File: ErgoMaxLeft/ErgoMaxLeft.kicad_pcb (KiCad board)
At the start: 2 copper layers, 182.8 x 169.2 mm, 102 parts, among them J1 PJ-320A, K1 KEYSW, K10 KEYSW, K11 KEYSW, K12 KEYSW, K13 KEYSW, K14 KEYSW, K15 KEYSW, K16 KEYSW, K17 KEYSW, K18 KEYSW, K19 KEYSW, K2 KEYSW, K20 KEYSW, K21 KEYSW, K22 KEYSW, K23 KEYSW, K24 KEYSW, K25 KEYSW, K26 KEYSW, K27 KEYSW, K28 KEYSW, K29 KEYSW, K3 KEYSW, K30 KEYSW, K31 KEYSW, K32 KEYSW, K33 KEYSW, K34 KEYSW, K35 KEYSW, K36 KEYSW, K37 KEYSW, K38 KEYSW, K39 KEYSW, K4 KEYSW, K40 KEYSW, K41 KEYSW, K42 KEYSW, K43 KEYSW, K44 KEYSW, K5 KEYSW, K6 KEYSW, K7 KEYSW, K8 KEYSW, K9 KEYSW, U1 ProMicro

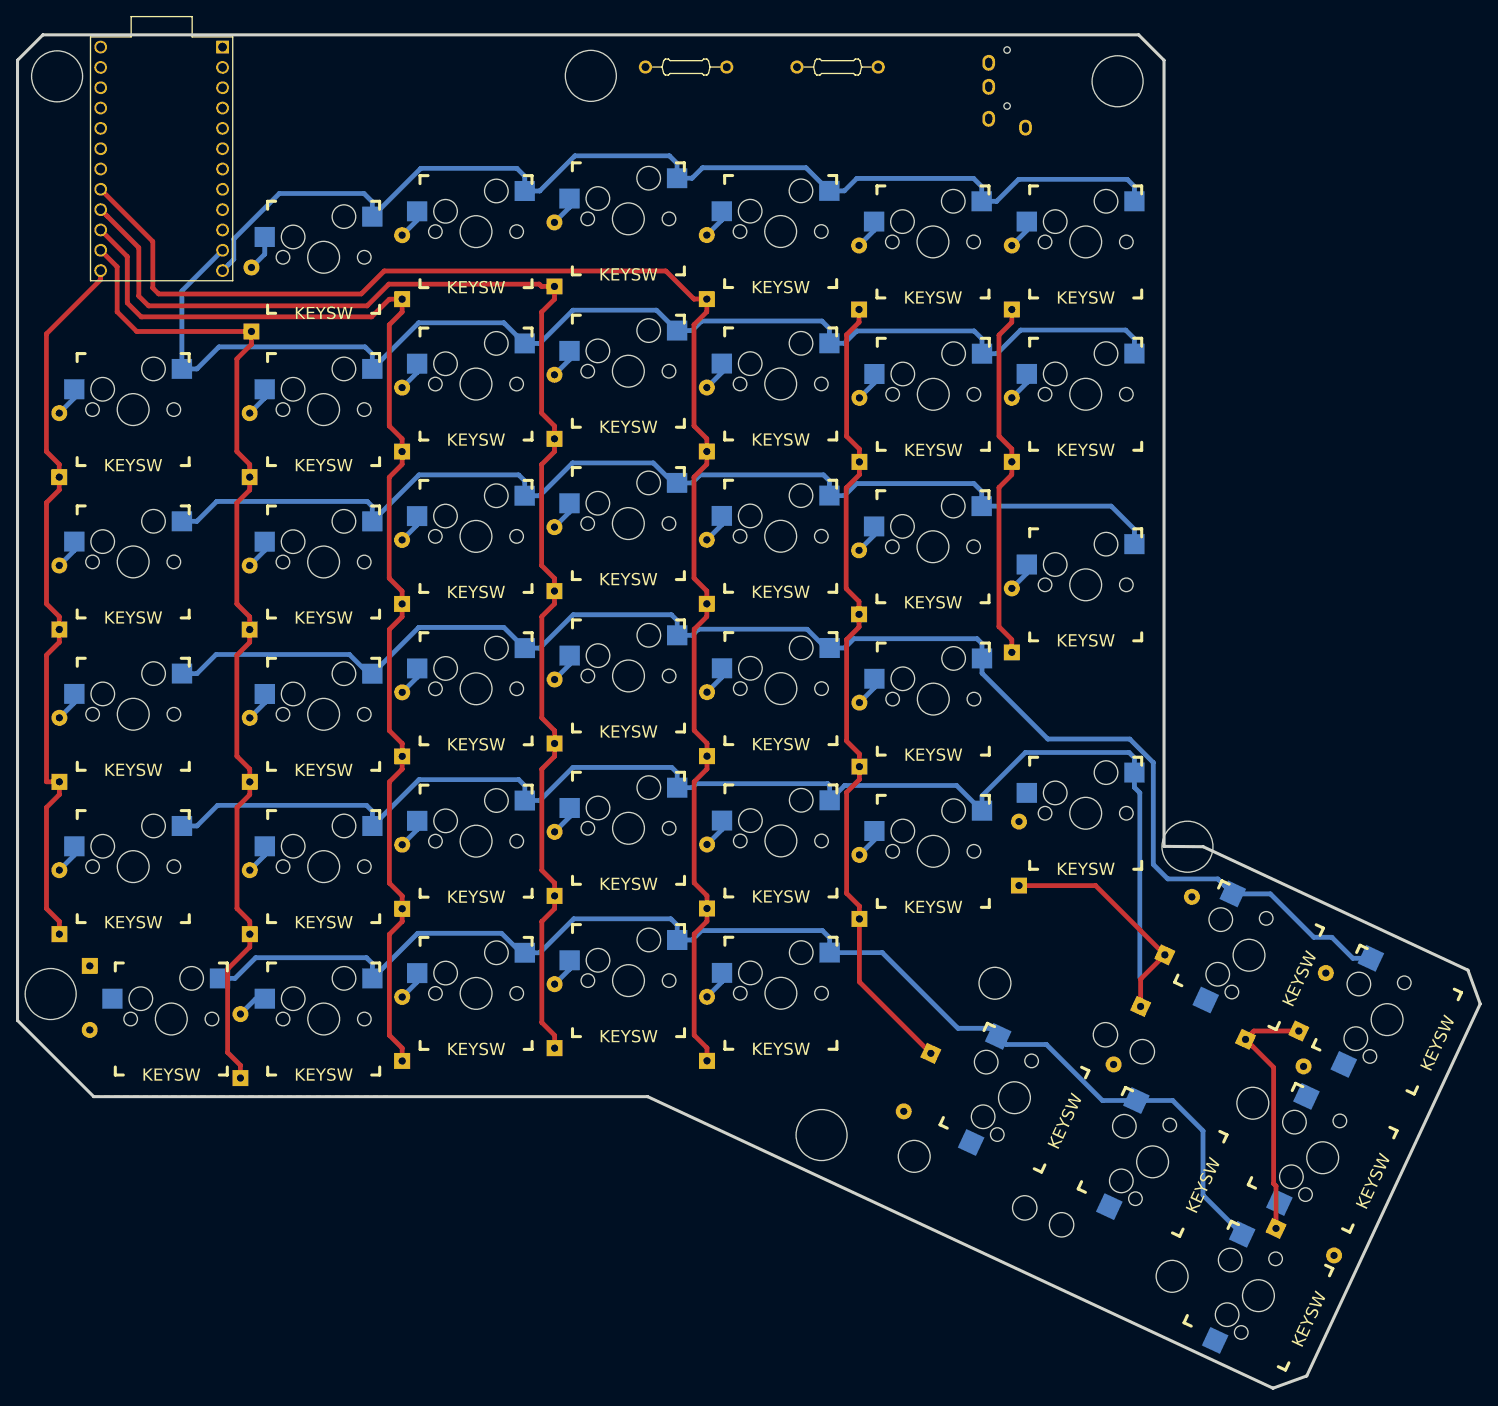
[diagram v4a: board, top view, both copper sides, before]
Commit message: finish left PCB and add 3d models
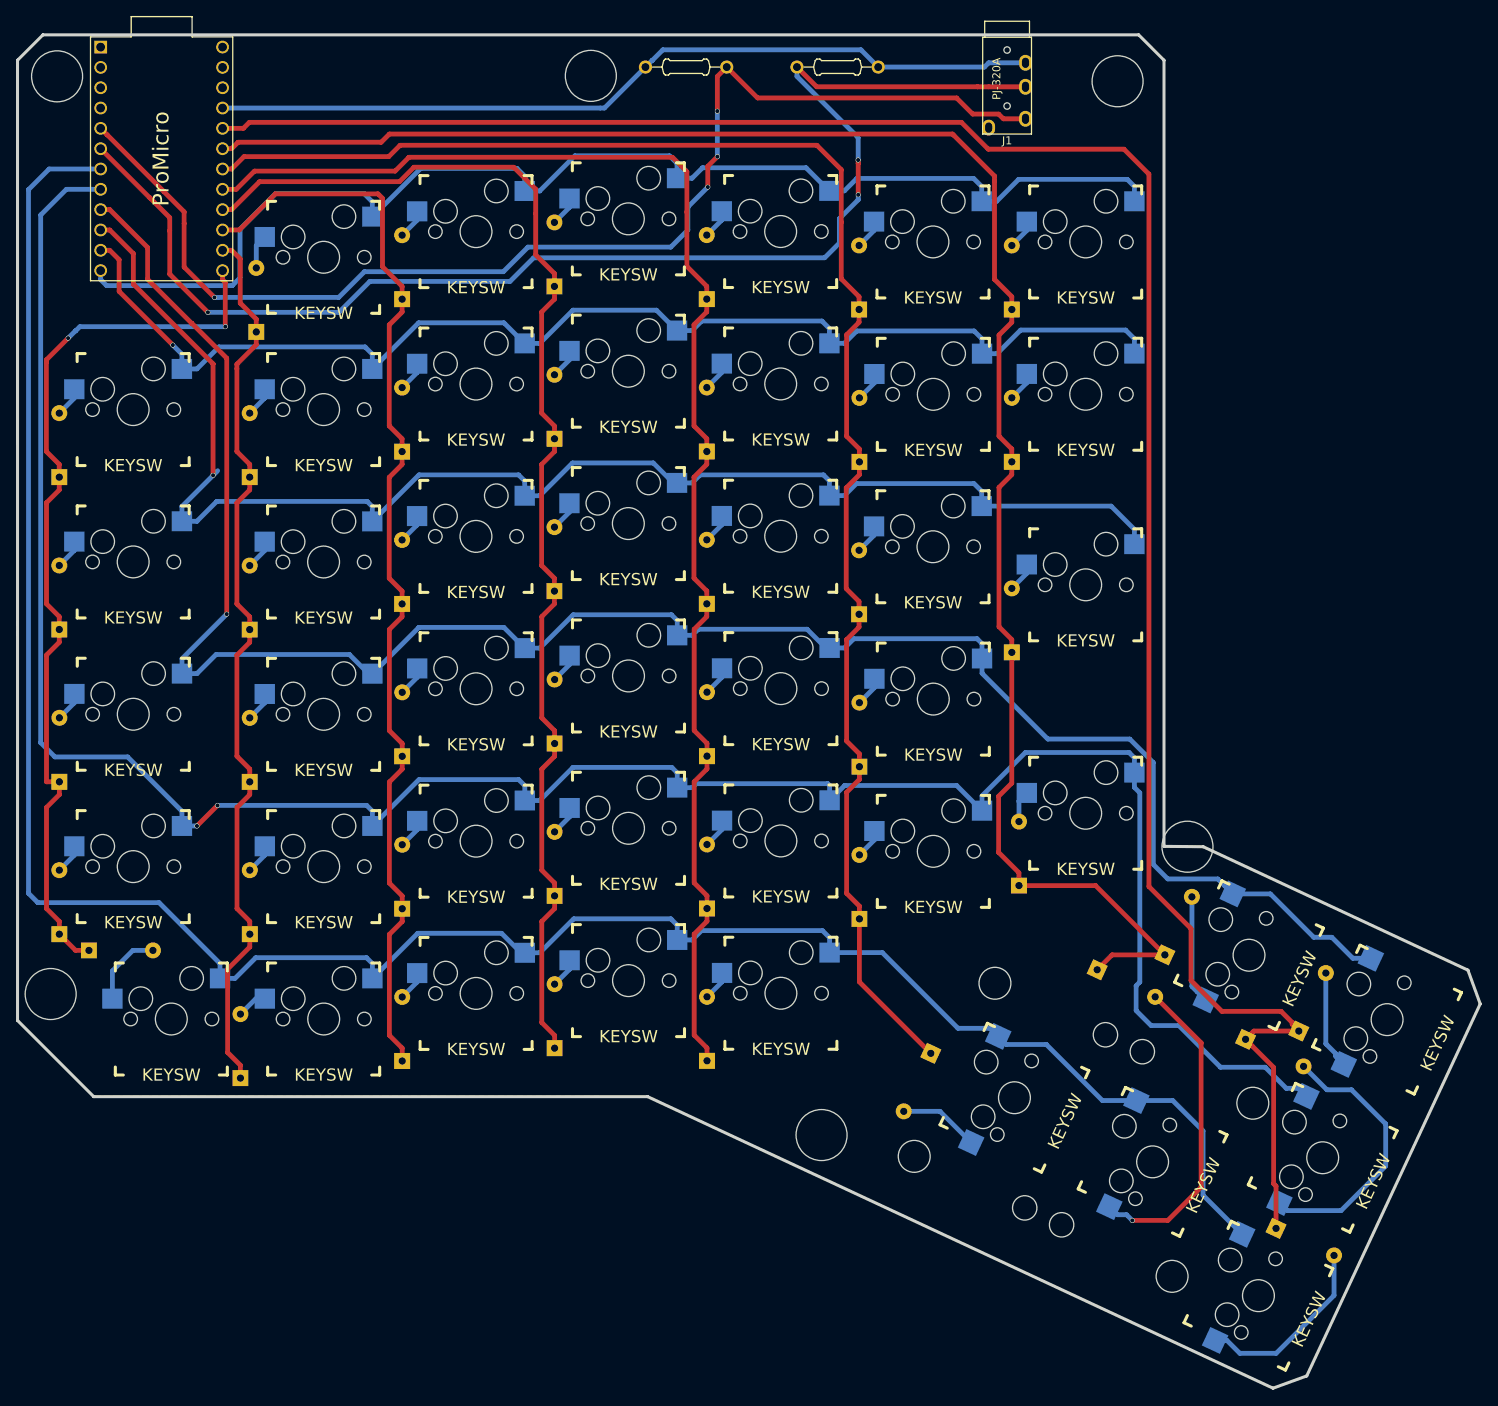
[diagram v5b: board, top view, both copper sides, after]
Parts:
- J1, U1: moved to F.Cu
- moved D37 7.11 mm to (123.3, 150.3), turned to 180 degrees
- moved D43 6.52 mm to (248.9, 154.4), turned to 155 degrees
- moved D1 0.61 mm to (140.2, 69.0)
- turned J1 to 0 degrees
- turned R2 to 180 degrees
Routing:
- net /Col7: track 32.3 -> 270.3 mm
- net SCL: track 0.00 -> 164.3 mm, vias 0 -> 3
- net SDA: track 0.00 -> 152.1 mm, vias 0 -> 4
- net /Col6: track 75.0 -> 224.5 mm
- net /Row4: track 167.0 -> 294.9 mm, vias 0 -> 2
- net /Row5: track 160.3 -> 287.8 mm
- net VCC: track 0.00 -> 104.5 mm
- net /Col5: track 102.0 -> 200.2 mm
- net /Row3: track 185.9 -> 253.4 mm, vias 0 -> 1
- net /Row2: track 138.0 -> 183.3 mm, vias 0 -> 1
- net Net-(D43-Pad2): track 0.00 -> 40.1 mm, vias 0 -> 1
- net Net-(D36-Pad2): track 0.00 -> 34.5 mm
- net Net-(D44-Pad2): track 0.00 -> 23.5 mm
- net /Col0: track 91.3 -> 113.1 mm, vias 0 -> 2
- net /Row0: track 138.6 -> 158.1 mm
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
